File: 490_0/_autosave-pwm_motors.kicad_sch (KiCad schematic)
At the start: 39 parts, among them J11 S2B-XH-A, J12 S2B-XH-A, J13 S2B-XH-A, J14 S2B-XH-A, J21 S2B-XH-A, Q3 NMOS, Q4 NMOS, Q5 NMOS, Q6 NMOS, Q7 NMOS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

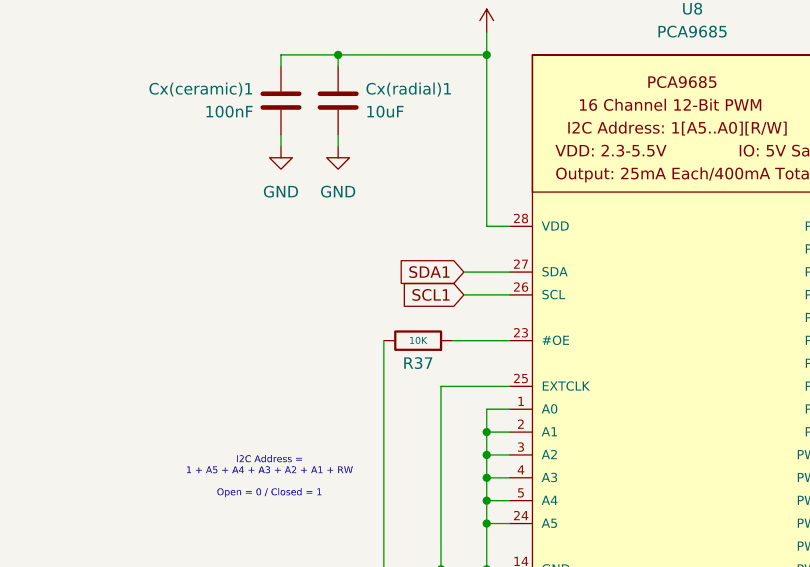
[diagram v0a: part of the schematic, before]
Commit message: Changed PCB block dagram and layout
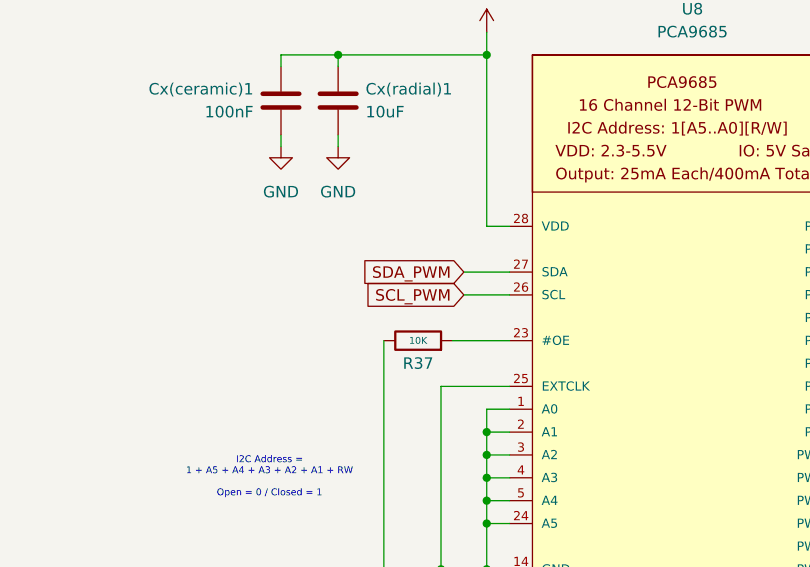
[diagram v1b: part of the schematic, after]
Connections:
- net SCL1 renamed SCL_PWM
- net SDA1 renamed SDA_PWM
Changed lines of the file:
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@@
 		)
 	)
-	(global_label "SCL1"
+	(global_label "SCL_PWM"
 		(shape input)
 		(at 81.28 158.75 180)
@@
 		)
 	)
-	(global_label "SDA1"
+	(global_label "SDA_PWM"
 		(shape input)
 		(at 81.28 156.21 180)
